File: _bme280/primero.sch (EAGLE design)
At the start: 3 parts

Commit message: Add files via upload
Este esquema hay que revisarlo, por si no está completo.
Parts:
- added 3V3: (no value), SparkFun-Connectors:CONN_02JST-PTH-2
- added C1: 100 nF, rcl:C-EUC0805
- added FLASH_P, RESET: (no value), switch-omron:10-XX
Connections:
- new net CSB: BME280.2
- new net GPIO0: FLASH_P.S, U$1.GPIO0
- new net RST: RESET.S, U$1.RST
- new net SCK_GPIO12: BME280.3, U$1.GPIO12
- new net SD0: BME280.1
- new net SDI_GPIO14: BME280.4, U$1.GPIO14
- new net XPD: U$1.GPIO16
- net GND: now also 3V3.2, BME280.5, C1.2, FLASH_P.P, RESET.P
- net VCC: now also 3V3.1, BME280.6, C1.1, U$1.VCC

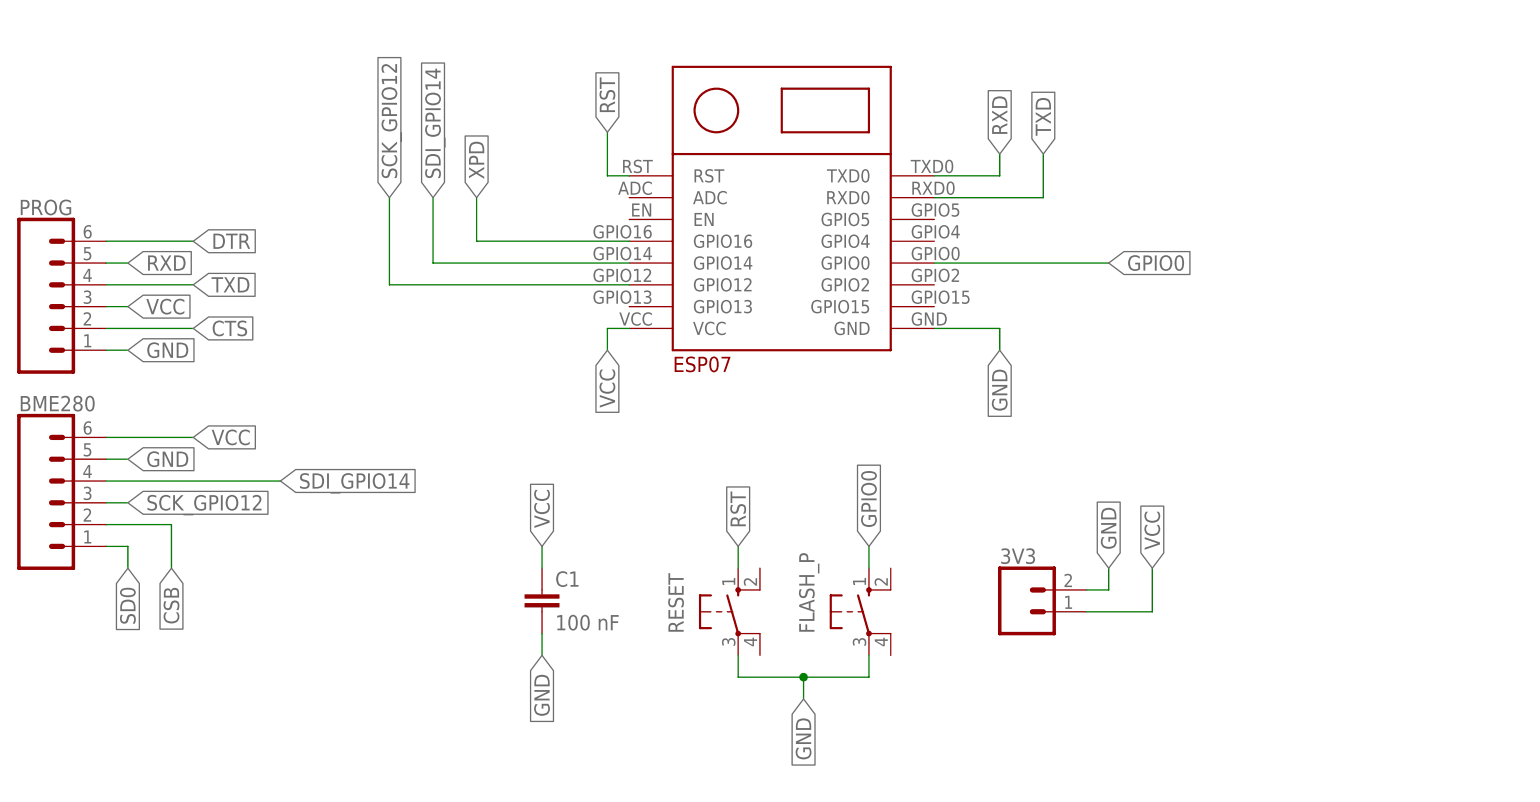
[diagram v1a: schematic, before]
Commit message: versión preliminar de PCB
-Añadido libreria:
https://github.com/wvanvlaenderen/ESP8266-Eagle_Library
- cambiados pulsadores a smd
-distribución inicial de pcb
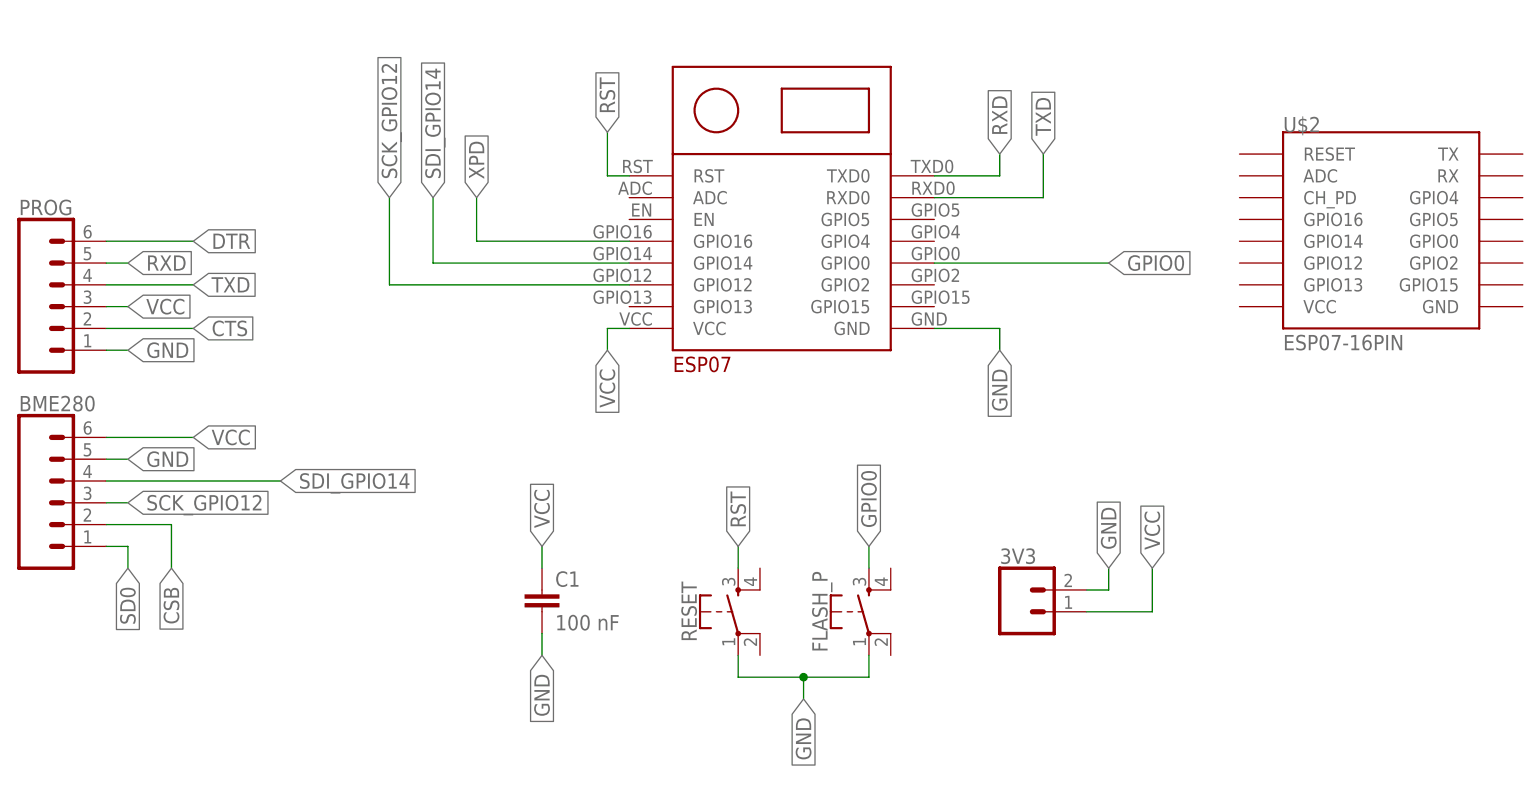
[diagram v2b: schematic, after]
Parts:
- added U$2: ESP07-16PIN, esp8266modules:ESP07-16PIN
- FLASH_P, RESET: device switch-omron:10-XX -> SparkFun-Switches:MOMENTARY-SWITCH-SPST-2-SMD-4.6X2.8MM
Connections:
- net GND: now also FLASH_P.1, RESET.1; no longer FLASH_P.P, RESET.P
- net GPIO0: now also FLASH_P.3; no longer FLASH_P.S
- net RST: now also RESET.3; no longer RESET.S
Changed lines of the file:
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@@
 <part name="PROG" library="SparkFun-Connectors" library_urn="urn:adsk.eagle:library:513" deviceset="CONN_06" device="SILK_FEMALE_PTH" package3d_urn="urn:adsk.eagle:package:38009/1"/>
 <part name="BME280" library="SparkFun-Connectors" library_urn="urn:adsk.eagle:library:513" deviceset="CONN_06" device="SILK_FEMALE_PTH" package3d_urn="urn:adsk.eagle:package:38009/1"/>
-<part name="RESET" library="switch-omron" library_urn="urn:adsk.eagle:library:377" deviceset="10-XX" device="" package3d_urn="urn:adsk.eagle:package:27496/1"/>
-<part name="FLASH_P" library="switch-omron" library_urn="urn:adsk.eagle:library:377" deviceset="10-XX" device="" package3d_urn="urn:adsk.eagle:package:27496/1"/>
 <part name="3V3" library="SparkFun-Connectors" library_urn="urn:adsk.eagle:library:513" deviceset="CONN_02" device="JST-PTH-2" package3d_urn="urn:adsk.eagle:package:38053/1"/>
 <part name="C1" library="rcl" library_urn="urn:adsk.eagle:library:334" deviceset="C-EU" device="C0805" package3d_urn="urn:adsk.eagle:package:23617/2" value="100 nF"/>
+<part name="RESET" library="SparkFun-Switches" library_urn="urn:adsk.eagle:library:535" deviceset="MOMENTARY-SWITCH-SPST-2" device="-SMD-4.6X2.8MM" package3d_urn="urn:adsk.eagle:package:40176/1"/>
+<part name="FLASH_P" library="SparkFun-Switches" library_urn="urn:adsk.eagle:library:535" deviceset="MOMENTARY-SWITCH-SPST-2" device="-SMD-4.6X2.8MM" package3d_urn="urn:adsk.eagle:package:40176/1"/>
+<part name="U$2" library="esp8266modules" deviceset="ESP07-16PIN" device=""/>
 </parts>
 <sheets>
@@
 <attribute name="NAME" x="7.62" y="61.468" size="1.778" layer="95" font="vector"/>
 </instance>
-<instance part="RESET" gate="1" x="91.44" y="38.1" smashed="yes">
-<attribute name="NAME" x="85.09" y="35.56" size="1.778" layer="95" rot="R90"/>
-<attribute name="VALUE" x="87.63" y="41.275" size="1.778" layer="96" rot="R90"/>
-</instance>
-<instance part="FLASH_P" gate="1" x="106.68" y="38.1" smashed="yes">
-<attribute name="NAME" x="100.33" y="35.56" size="1.778" layer="95" rot="R90"/>
-<attribute name="VALUE" x="102.87" y="41.275" size="1.778" layer="96" rot="R90"/>
-</instance>
 <instance part="3V3" gate="G$1" x="124.46" y="38.1" smashed="yes">
 <attribute name="VALUE" x="121.92" y="33.274" size="1.778" layer="96" font="vector"/>
@@
 <attribute name="NAME" x="70.104" y="41.021" size="1.778" layer="95"/>
 <attribute name="VALUE" x="70.104" y="35.941" size="1.778" layer="96"/>
+</instance>
+<instance part="RESET" gate="G$1" x="91.44" y="38.1" smashed="yes" rot="R90">
+<attribute name="NAME" x="86.614" y="38.1" size="1.778" layer="95" font="vector" rot="R90" align="bottom-center"/>
+<attribute name="VALUE" x="94.234" y="38.1" size="1.778" layer="96" font="vector" rot="R90" align="top-center"/>
+</instance>
+<instance part="FLASH_P" gate="G$1" x="106.68" y="38.1" smashed="yes" rot="R90">
+<attribute name="NAME" x="101.854" y="38.1" size="1.778" layer="95" font="vector" rot="R90" align="bottom-center"/>
+<attribute name="VALUE" x="109.474" y="38.1" size="1.778" layer="96" font="vector" rot="R90" align="top-center"/>
+</instance>
+<instance part="U$2" gate="G$1" x="167.64" y="83.82" smashed="yes">
+<attribute name="NAME" x="154.94" y="93.98" size="1.778" layer="95"/>
+<attribute name="VALUE" x="154.94" y="68.58" size="1.778" layer="96"/>
 </instance>
 </instances>
@@
 <segment>
 <label x="99.06" y="27.94" size="1.778" layer="95" rot="R270" xref="yes"/>
-<pinref part="FLASH_P" gate="1" pin="P"/>
 <wire x1="106.68" y1="33.02" x2="106.68" y2="30.48" width="0.1524" layer="91"/>
-<pinref part="RESET" gate="1" pin="P"/>
 <wire x1="91.44" y1="33.02" x2="91.44" y2="30.48" width="0.1524" layer="91"/>
 <wire x1="91.44" y1="30.48" x2="99.06" y2="30.48" width="0.1524" layer="91"/>
@@
 <wire x1="99.06" y1="27.94" x2="99.06" y2="30.48" width="0.1524" layer="91"/>
 <junction x="99.06" y="30.48"/>
+<pinref part="RESET" gate="G$1" pin="1"/>
+<pinref part="FLASH_P" gate="G$1" pin="1"/>
 </segment>
 <segment>
@@
 </segment>
 <segment>
-<pinref part="RESET" gate="1" pin="S"/>
 <wire x1="91.44" y1="43.18" x2="91.44" y2="45.72" width="0.1524" layer="91"/>
 <label x="91.44" y="45.72" size="1.778" layer="95" rot="R90" xref="yes"/>
+<pinref part="RESET" gate="G$1" pin="3"/>
 </segment>
 </net>
@@
 </segment>
 <segment>
-<pinref part="FLASH_P" gate="1" pin="S"/>
 <wire x1="106.68" y1="43.18" x2="106.68" y2="45.72" width="0.1524" layer="91"/>
 <label x="106.68" y="45.72" size="1.778" layer="95" rot="R90" xref="yes"/>
-</segment>
-</net>
+<pinref part="FLASH_P" gate="G$1" pin="3"/>
+</segment>
+</net>
